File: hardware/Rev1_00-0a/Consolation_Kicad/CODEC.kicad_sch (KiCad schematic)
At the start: 25 parts, among them J2 SJ-3524-SMT-TR, U4 ECS-2016MVQ-120-BP-TR, U5 NAU88C22YG, U6 AP22913W6-7

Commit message: Update schematics, block diagram and pin mux (good progress G)
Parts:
- added J10, J8: 0532610271, footprint:0532610271, symbol KicadCompDb:Connector/CONN_00027
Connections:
- net GND: now also U5.24 (VSSSPK), J10.1, J8.1
- net LSPKOUT: now also J8.2
- net RSPKOUT: now also J10.2
- net 3V3_CB renamed 3V3
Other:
- note added: "LSPK"
- note added: "RSPK"
- note added: "Speaker connector orientation"
- moved on the sheet: C11, C12, C216, C217, C218, C219, C220, C221, C222, C223, C224, C225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

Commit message: Update PinMux & Schematics
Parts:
- removed C227: 0.1u, footprint:CAP_NONPOL_0402, symbol KicadCompDb:Capacitors/CAP_CER_SMT_00001
- removed U6: AP22913W6-7, footprint:SOT-23-6, symbol KicadCompDb:Load Switch/LOAD_SW_00001
- added R21: 33K, footprint:RES_0402, symbol KicadCompDb:Resistors/RES_SMT_00031
- added X1, X2: CMS-241535-078L65, symbol KicadCompDb:Miscellaneous/MISC_00014
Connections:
- net CODEC_3V3 is gone; now on net 3V3: C216.2, C220.2, C221.2, C222.2, C223.2, C224.2, C225.2, C226.2, U5.13 (VDDC), U5.14 (VDDB), U5.26 (VDDSPK), U5.31 (VDDA)
- net ~{HP_DETECT} is gone; now on net HEADPHONE_DETECT: J2.4 (SW)
- net 3V3: now also R21.2
- net HEADPHONE_DETECT: now reaches U5.3 (LLIN)
- net HEADPHONE_DETECT: now also R21.1
- net CODEC_CLK_12MHz: no longer names the net of R277.2, U5.11 (MCLK)
- no-connect marks 11 -> 10
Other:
- moved on the sheet: C217, C218, C219, D45, J10, J8, R277, R279, U4

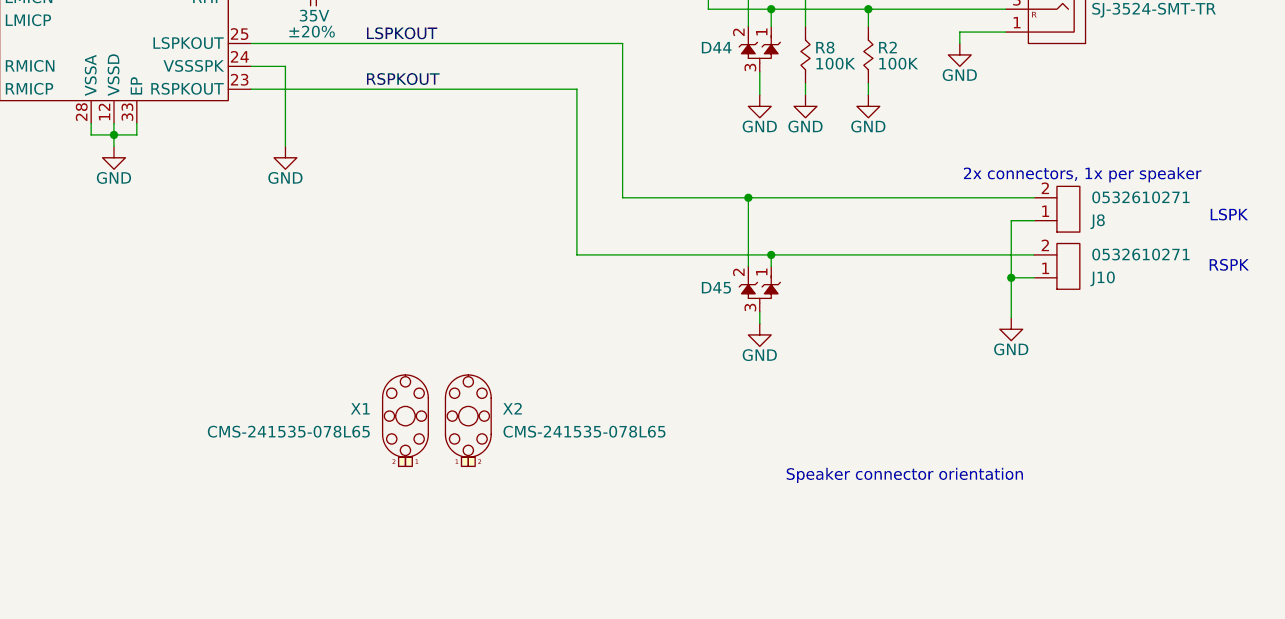
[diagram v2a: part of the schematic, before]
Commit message: Work on ConJoy [Consolation Joycon] Work on Consolation [Console Emulation]
- Adjust controller pinout
- Design controller for 1-PCB fits both side (reversible design for L-R controller)
- Preliminary PCB for 3d modeling
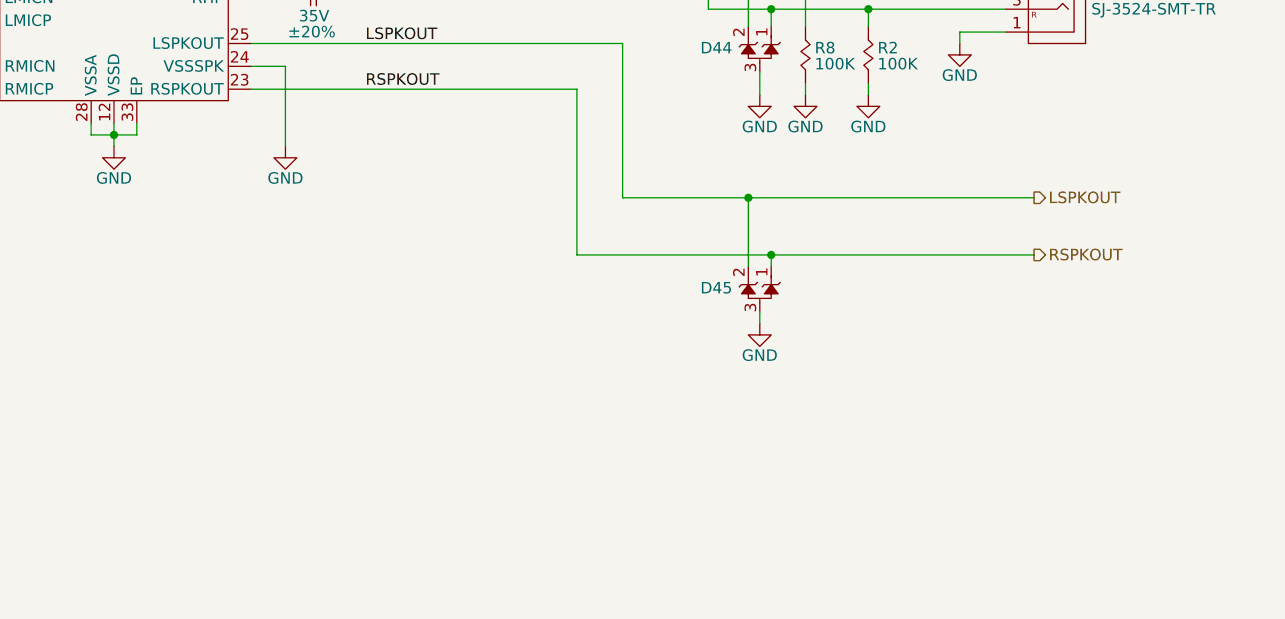
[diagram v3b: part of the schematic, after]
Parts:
- removed J10, J8: 0532610271, footprint:0532610271, symbol KicadCompDb:Connector/CONN_00027
- removed X1, X2: CMS-241535-078L65, symbol KicadCompDb:Miscellaneous/MISC_00014
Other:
- note removed: "2x connectors, 1x per speaker"
- note removed: "LSPK"
- note removed: "RSPK"
- note removed: "Speaker connector orientation"

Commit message: Major update to consolation schematics to include - Power supply - RESET SUPERVISOR - Review of GPIO and pinmux
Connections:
- net CODEC_~{RST} renamed ~{CODEC_RST}
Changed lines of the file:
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@@
 	(title_block
 		(title "Consolation [Console Emulation]")
-		(date "2026-08-03")
-		(rev "1.00-0a")
+		(date "2026-08-08")
+		(rev "1.00-0A")
 		(comment 1 "Jean-Francois Bilodeau")
 		(comment 2 "P.Eng #6022173")
@@
 		)
 	)
-	(hierarchical_label "CODEC_~{RST}"
+	(hierarchical_label "~{CODEC_RST}"
 		(shape input)
 		(at 31.75 62.865 180)
@@
 		)
 		(property "Frequency" "12MHz"
-			(at 62.865 61.595 0)
-			(hide yes)
-			(show_name yes)
+			(at 67.818 65.278 0)
+			(show_name no)
 			(do_not_autoplace no)
 			(effects
@@
 		)
 		(property "Manufacturer Part Number" "ECS-2016MVQ-120-BP-TR"
-			(at 62.865 61.595 0)
-			(hide yes)
-			(show_name yes)
+			(at 74.422 70.104 0)
+			(show_name no)
 			(do_not_autoplace no)
 			(effects

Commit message: Removed unnecessary functions (USB2 mux, CapTouch) Adjusted 220uF alum capacitor for codec (slimmer version)
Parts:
- removed C11, C12: 220u, footprint:CAP_ALU_8mm_10.5mm, symbol KicadCompDb:Capacitors/CAP_ALU_SMT_00018
- added C11, C12: 220u, footprint:CAP_ALU_6_3mm_6_10mm, symbol KicadCompDb:Capacitors/CAP_ALU_SMT_00020
- added R278: 22R, footprint:RES_0402, symbol KicadCompDb:Resistors/RES_SMT_00015
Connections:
- net HEADPHONE_DETECT: now also R278.2; no longer J2.4 (SW), R21.1
- net HP_L_OUT: now also C11.2
- net HP_R_OUT: now also C12.2
- net at U5.29 (RHP): now also C12.1
- net at U5.30 (LHP): now also C11.1
- new net: J2.4 (SW), R21.1, R278.1

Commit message: Component preliminary placement
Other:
- moved on the sheet: C11, C12, C216, C217, C218, C219, C220, C221, C222, C223, C224, C225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

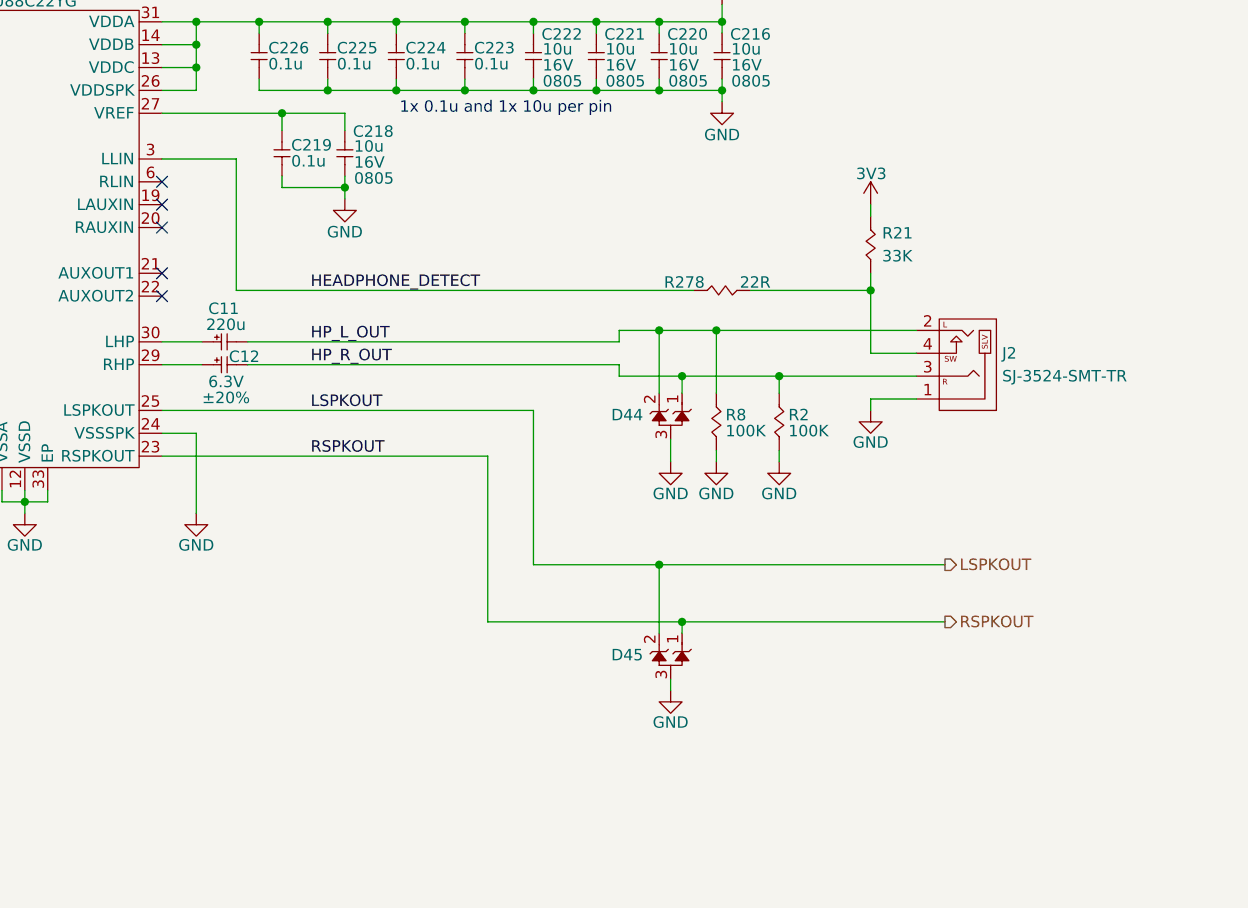
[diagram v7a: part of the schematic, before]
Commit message: Preliminary placement of Consolation continues
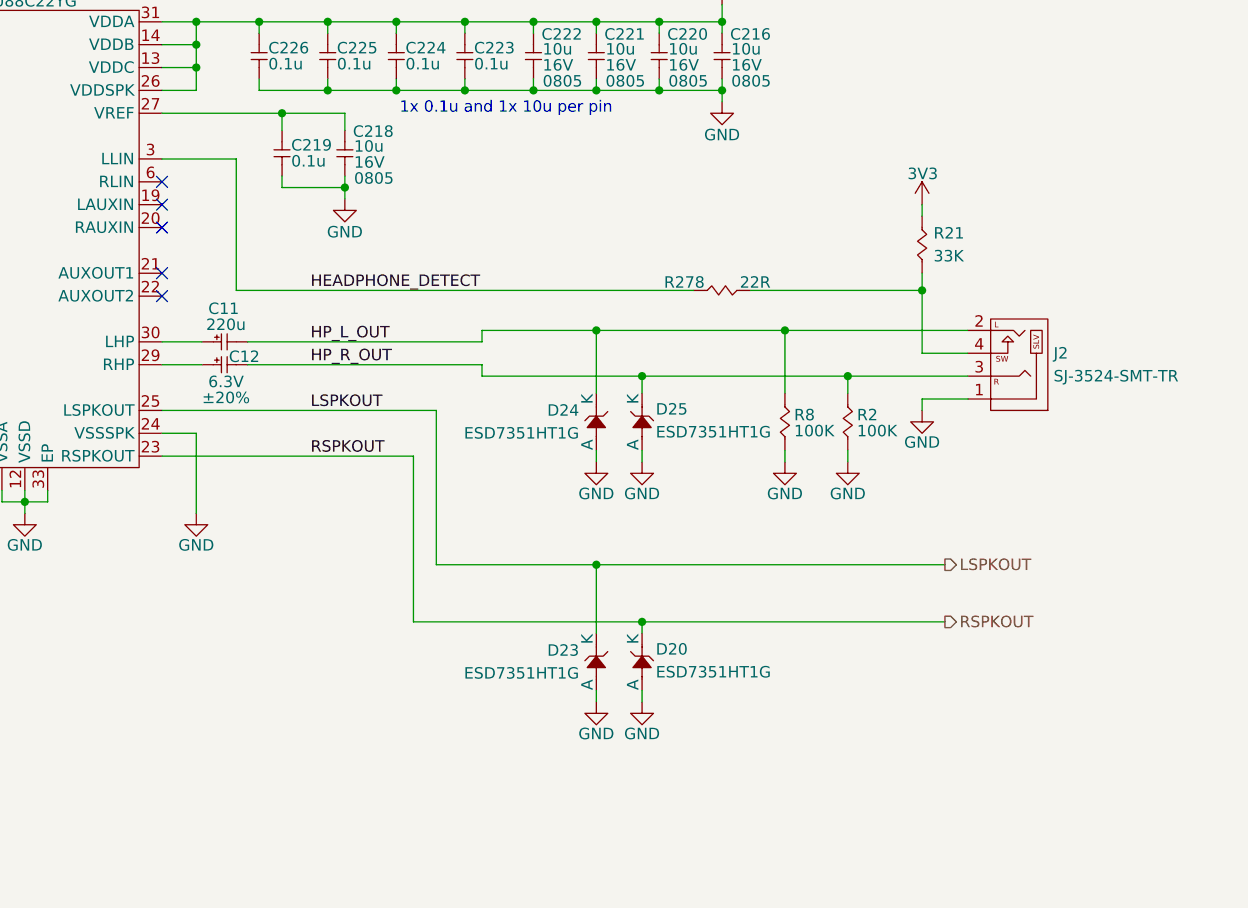
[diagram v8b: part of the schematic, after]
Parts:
- removed D44, D45: D1213A-02SOL-7, footprint:SOT-23-3, symbol KicadCompDb:ESD Diodes/ESD_DIODE_00002
- added D20, D23, D24, D25: ESD7351HT1G, footprint:SOD-323, symbol KicadCompDb:ESD Diodes/ESD_DIODE_00006
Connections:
- net GND: now also D20.2 (A), D23.2 (A), D24.2 (A), D25.2 (A)
- net HP_L_OUT: now also D24.1 (K)
- net HP_R_OUT: now also D25.1 (K)
- net LSPKOUT: now also D23.1 (K)
- net RSPKOUT: now also D20.1 (K)
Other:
- moved on the sheet: J2, R2, R21, R8
